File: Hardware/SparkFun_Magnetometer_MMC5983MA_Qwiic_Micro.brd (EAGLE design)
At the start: 19.1 x 8.9 mm, 35 parts, among them J1 QWIIC_RIGHT_ANGLE, U2 MMC5983MA_QFN16

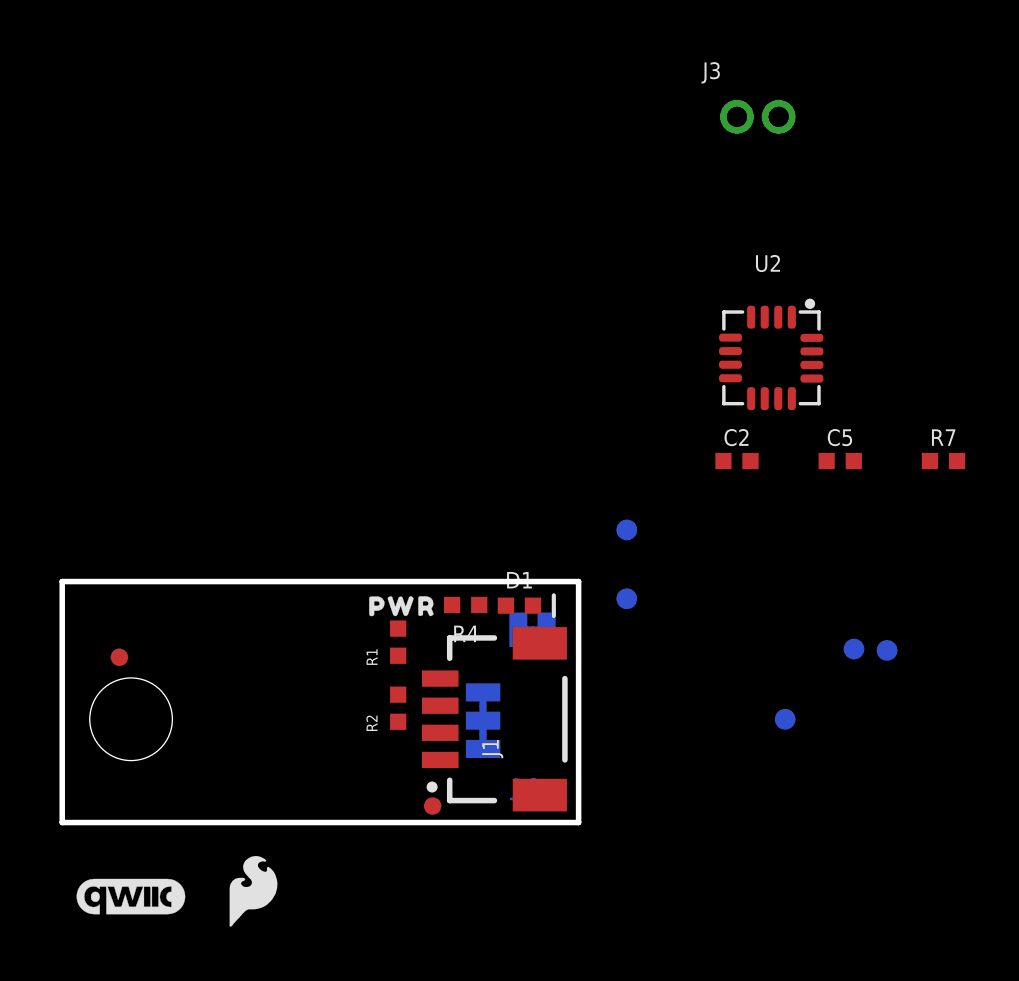
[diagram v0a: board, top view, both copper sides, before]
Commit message: Places parts, fixes some schematic alignment issues
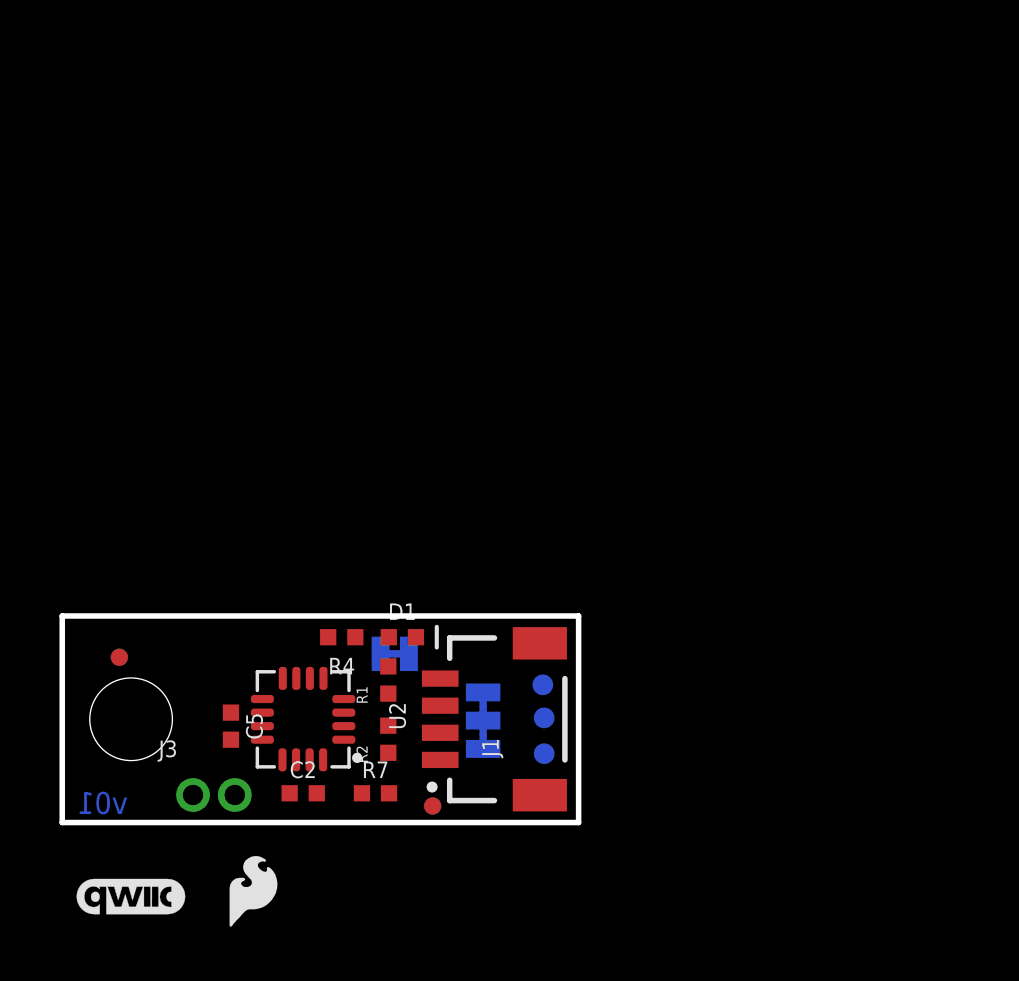
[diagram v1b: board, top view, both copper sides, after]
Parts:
- removed U$28: (no value), top:PWR8
- moved J3 32.1 mm to (4.83, 1.02)
- moved C5 24.5 mm to (6.22, 3.56), turned to 270 degrees
- moved R7 24.3 mm to (11.6, 1.08)
- moved U2 21.8 mm to (8.89, 3.81), turned to 270 degrees
- moved C2 20.2 mm to (8.89, 1.08)
- moved TP3 12.8 mm to (17.7, 5.08)
- moved TP2 11.7 mm to (17.8, 3.86)
- moved TP1 8.98 mm to (17.8, 2.54)
- moved TP5 7.85 mm to (17.8, 1.02)
- moved TP4 5.18 mm to (17.8, 6.60)
- moved LED 5.16 mm to (12.3, 6.22)
- moved R4 4.72 mm to (10.3, 6.84)
- moved D1 4.47 mm to (12.5, 6.84)
- moved R1 1.44 mm to (12.0, 5.26)
- moved R2 1.20 mm to (12.0, 3.07)
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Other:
- board size 19.1 x 8.9 mm -> 19.1 x 7.6 mm

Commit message: Adds measures
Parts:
- moved LOGO1 27.5 mm to (23.9, 14.5)
- moved U$29 27.5 mm to (28.4, 14.8)
- moved FRAME1 7.62 mm to (-18.8, -19.1)
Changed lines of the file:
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@@
 <setting verticaltext="up"/>
 </settings>
-<grid distance="0.05" unitdist="inch" unit="inch" style="dots" multiple="1" display="yes" altdistance="0.005" altunitdist="inch" altunit="inch"/>
+<grid distance="0.01" unitdist="inch" unit="inch" style="dots" multiple="1" display="yes" altdistance="0.005" altunitdist="inch" altunit="inch"/>
 <layers>
 <layer number="1" name="Top" color="4" fill="1" visible="yes" active="yes"/>
@@
 <layer number="45" name="Holes" color="7" fill="1" visible="yes" active="yes"/>
 <layer number="46" name="Milling" color="3" fill="1" visible="no" active="yes"/>
-<layer number="47" name="Measures" color="7" fill="1" visible="no" active="yes"/>
+<layer number="47" name="Measures" color="7" fill="1" visible="yes" active="yes"/>
 <layer number="48" name="Document" color="7" fill="1" visible="no" active="yes"/>
 <layer number="49" name="Reference" color="13" fill="1" visible="yes" active="yes"/>
@@
 <wire x1="19.05" y1="0" x2="19.05" y2="7.62" width="0.2032" layer="20"/>
 <text x="2.422525" y="0.314325" size="0.8128" layer="16" font="vector" ratio="22" rot="MR0">v01</text>
-<dimension x1="0" y1="8.89" x2="0" y2="0" x3="-8.636" y3="4.445" textsize="1.778" textratio="15" layer="47" unit="inch" visible="yes"/>
-<dimension x1="19.05" y1="8.89" x2="0" y2="8.89" x3="9.525" y3="22.86" textsize="1.778" textratio="15" layer="47" unit="inch" visible="yes"/>
 <rectangle x1="8.89" y1="3.4036" x2="8.9408" y2="3.7084" layer="41"/>
 <wire x1="14.2494" y1="4.752975" x2="12.3444" y2="4.752975" width="0.254" layer="22"/>
@@
 <wire x1="10.8204" y1="5.334" x2="12.0904" y2="4.064" width="0.254" layer="22"/>
 <dimension x1="13.9446" y1="3.81" x2="13.97" y2="0" x3="25.4" y3="1.905" textsize="1.778" layer="47" dtype="vertical" unit="inch"/>
-<dimension x1="2.54" y1="3.81" x2="2.54" y2="0" x3="-12.7" y3="1.905" textsize="1.778" layer="47" dtype="vertical" unit="inch"/>
-<dimension x1="6.4008" y1="7.6708" x2="0" y2="7.62" x3="3.2004" y3="11.43" textsize="1.778" layer="47" dtype="horizontal" unit="inch"/>
+<dimension x1="19.05" y1="7.62" x2="0" y2="7.62" x3="9.525" y3="16.764" textsize="1.778" layer="47" dtype="horizontal" unit="inch"/>
+<dimension x1="0" y1="7.62" x2="0" y2="0" x3="-6.096" y3="3.81" textsize="1.778" layer="47" dtype="horizontal" unit="inch"/>
+<dimension x1="8.89" y1="3.81" x2="0" y2="4.064" x3="4.445" y3="12.7" textsize="1.778" layer="47" dtype="horizontal" unit="inch"/>
+<dimension x1="2.54" y1="3.81" x2="0" y2="4.064" x3="1.27" y3="-3.302" textsize="1.778" layer="47" dtype="horizontal" unit="inch"/>
+<dimension x1="4.826" y1="1.016" x2="0" y2="1.016" x3="2.413" y3="-6.35" textsize="1.778" layer="47" dtype="horizontal" unit="inch"/>
+<dimension x1="4.826" y1="1.016" x2="4.826" y2="0" x3="-1.27" y3="0.508" textsize="1.778" layer="47" dtype="vertical" unit="inch"/>
 </plain>
 <attributes>
@@
 </autorouter>
 <elements>
-<element name="FRAME1" library="SparkFun-Aesthetics" package="CREATIVE_COMMONS" value="FRAME-LETTER" x="-19.05" y="-11.43" smashed="yes">
-<attribute name="DESIGNER" value="Elias Santistevan" x="12.7" y="-11.43" size="1.778" layer="51" font="vector"/>
-<attribute name="REV" value="" x="-19.05" y="-11.43" size="1.778" layer="27" display="off"/>
+<element name="FRAME1" library="SparkFun-Aesthetics" package="CREATIVE_COMMONS" value="FRAME-LETTER" x="-18.796" y="-19.05" smashed="yes">
+<attribute name="DESIGNER" value="Elias Santistevan" x="12.954" y="-19.05" size="1.778" layer="51" font="vector"/>
+<attribute name="REV" value="" x="-18.796" y="-19.05" size="1.778" layer="27" display="off"/>
 </element>
 <element name="LOGO2" library="SparkFun-Aesthetics" package="OSHW-LOGO-MINI" value="OSHW-LOGOMINI" x="1.4224" y="1.20015" smashed="yes" rot="MR0"/>
@@
 <element name="FD1" library="SparkFun-Aesthetics" package="FIDUCIAL-MICRO" value="FIDUCIALUFIDUCIAL" x="2.1082" y="6.096" smashed="yes" rot="MR0"/>
 <element name="FD2" library="SparkFun-Aesthetics" package="FIDUCIAL-MICRO" value="FIDUCIALUFIDUCIAL" x="13.6652" y="0.6096" smashed="yes" rot="MR0"/>
-<element name="LOGO1" library="SparkFun-Aesthetics" package="QWIIC_4MM" value="QWIIC_LOGO_4MM" x="2.54" y="-2.7432" smashed="yes"/>
+<element name="LOGO1" library="SparkFun-Aesthetics" package="QWIIC_4MM" value="QWIIC_LOGO_4MM" x="23.876" y="14.5288" smashed="yes"/>
 <element name="D1" library="ISM330DHCX" package="0402-TIGHT" value="RED" x="12.5476" y="6.838340625" smashed="yes">
 <attribute name="NAME" x="12.5476" y="7.473340625" size="0.6096" layer="25" font="vector" ratio="20" align="bottom-center"/>
@@
 <attribute name="VALUE" x="12.2682" y="7.366" size="0.6096" layer="28" font="vector" ratio="20" rot="MR180" align="top-center"/>
 </element>
-<element name="U$29" library="SparkFun-Aesthetics" package="SFE_LOGO_FLAME_.1" value="" x="7.0358" y="-2.5146" smashed="yes"/>
+<element name="U$29" library="SparkFun-Aesthetics" package="SFE_LOGO_FLAME_.1" value="" x="28.3718" y="14.7574" smashed="yes"/>
 <element name="U$8" library="ISMTopMini" package="X2114" value="" x="13.0302" y="4.0132" smashed="yes" rot="MR0"/>
 <element name="U$9" library="ISMTopMini" package="Y2115" value="" x="11.9484" y="2.9718" smashed="yes" rot="MR0"/>

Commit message: Routes the board
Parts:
- removed TP4: TEST-POINT3, SparkFun-Connectors:PAD.03X.03
- moved U$29 29.3 mm to (2.39, 1.12), turned to 90 degrees
- moved LOGO1 22.0 mm to (3.38, 6.58)
- moved FD1 1.62 mm to (0.71, 6.91)
- moved FID1 1.62 mm to (0.71, 6.91)
- moved LED 0.49 mm to (12.7, 6.50)
- moved C2 0.26 mm to (8.64, 1.03)
- moved R7 0.23 mm to (11.8, 1.03)
- moved R2 0.08 mm to (12.1, 3.15), turned to 270 degrees
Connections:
- net INT: no longer TP4.1
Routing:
- net 3.3V: track 0.00 -> 24.5 mm, vias 0 -> 4
- net SDA: track 0.00 -> 10.4 mm, vias 0 -> 1
- net SCL: track 0.00 -> 8.81 mm, vias 0 -> 1
- net !MAG_CS!: track 0.00 -> 5.37 mm, vias 0 -> 2
- net INT: track 0.00 -> 4.61 mm
- net N$5: track 0.00 -> 4.52 mm, vias 0 -> 1
- net N$6: track 0.00 -> 3.50 mm, vias 0 -> 1
- net N$3: track 0.00 -> 2.38 mm, vias 0 -> 1
- net N$2: track 0.00 -> 1.24 mm
- net GND: track 0.00 -> 0.73 mm, vias 0 -> 6
- added copper zone on layer 1, net 3.3V
- added copper zone on layer 1, net CAP

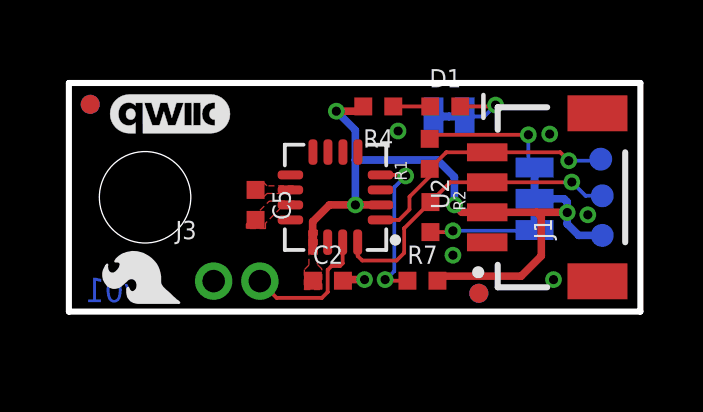
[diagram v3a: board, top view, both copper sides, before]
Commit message: Adds Silk, moves testpoints to grid, updates two pin connector
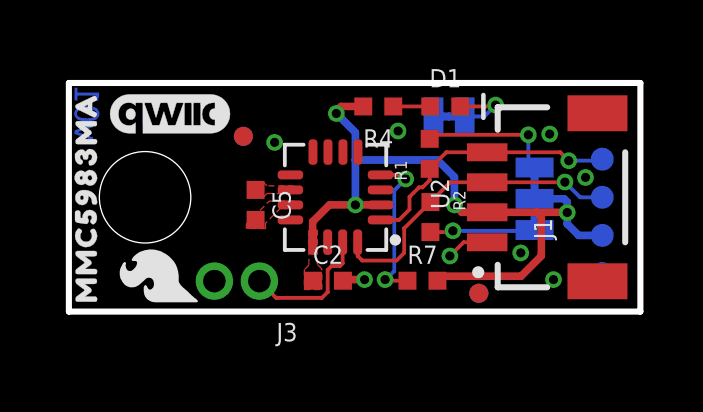
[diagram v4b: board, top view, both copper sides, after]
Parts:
- removed LOGO3: SFE_LOGO_NAMEBLANK, SparkFun-Aesthetics:BLANK
- added U$1, U$2: (no value), topMini:MMC5983MA331
- moved FD1 5.22 mm to (5.82, 5.84)
- moved FID1 5.22 mm to (5.82, 5.84)
- moved U$5 5.09 mm to (4.88, 2.91), turned to 90 degrees
- moved U$6 3.90 mm to (6.30, 2.71), turned to 90 degrees
- moved U$8 3.70 mm to (9.45, 4.95), turned to 270 degrees
- moved U$9 3.21 mm to (8.74, 2.81), turned to 90 degrees
- moved U$3 3.03 mm to (14.1, 3.84)
- moved U$10 2.45 mm to (11.6, 3.61), turned to 90 degrees
- moved J3 1.52 mm to (6.35, 1.02), turned to 180 degrees
- moved U$4 0.71 mm to (15.3, 6.60), turned to 180 degrees
- moved U$29 0.59 mm to (2.97, 1.17)
- moved TP5 0.25 mm to (17.8, 1.27)
- moved TP3 0.05 mm to (17.8, 5.08)
- moved TP2 0.05 mm to (17.8, 3.81)
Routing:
- net GND: track 0.73 -> 2.17 mm, vias 6 -> 8

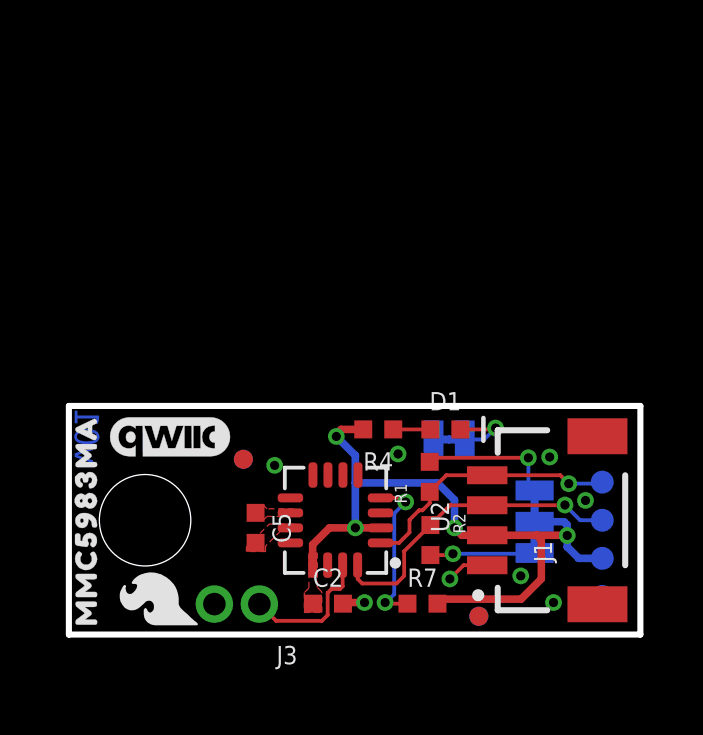
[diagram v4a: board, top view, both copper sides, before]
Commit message: Moves interrupt and ground pins, fixes silk, moves testpoints to 0.0375" grid
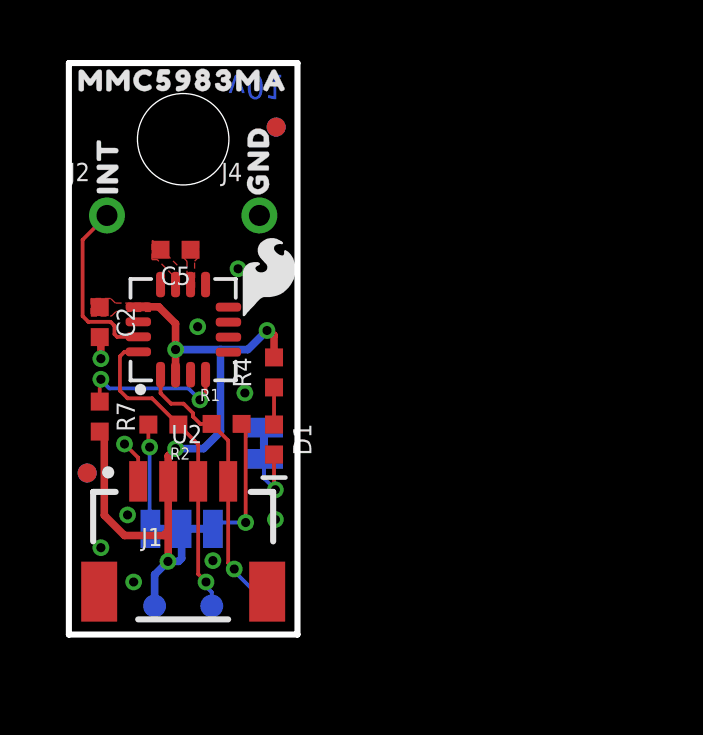
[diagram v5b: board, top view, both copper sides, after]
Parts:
- removed J3: (no value), SparkFun-Connectors:1X02_1.5MM_NO_SILK
- added J2, J4: (no value), SparkFun-Connectors:1X01_1MM_NO_SILK
- U$4: device LISMini:#LED#7 -> topMini:#LED#15
- moved TP5 16.8 mm to (0.95, 0.95), turned to 90 degrees
- moved LOGO2 16.4 mm to (1.20, 17.6), turned to 90 degrees
- moved TP1 15.0 mm to (2.86, 0.95), turned to 90 degrees
- moved U$1 15.0 mm to (3.81, 18.5), turned to 0 degrees
- moved FD2 13.9 mm to (0.61, 5.38), turned to 90 degrees
- moved FID2 13.9 mm to (0.61, 5.38), turned to 270 degrees
- moved U$6 13.9 mm to (1.29, 15.6), flipped to the top
- moved TP2 13.3 mm to (4.76, 0.95), turned to 90 degrees
- moved U$5 13.0 mm to (6.32, 15.8), flipped to the top
- moved STANDOFF3 12.8 mm to (3.81, 16.5), turned to 270 degrees
- moved R7 12.4 mm to (1.03, 7.26), turned to 270 degrees
- moved C2 12.1 mm to (1.03, 10.4), turned to 270 degrees
- moved TP3 11.9 mm to (6.67, 0.95), turned to 90 degrees
- moved I2C_PU 11.8 mm to (3.76, 3.52), turned to 0 degrees
- moved U$29 11.4 mm to (6.65, 11.9), turned to 0 degrees
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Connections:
- net GND: now also J4.1; no longer J3.1
- net INT: now also J2.1; no longer J3.2
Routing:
- net INT: track 4.62 -> 6.00 mm
- net SCL: track 8.93 -> 9.67 mm
- net GND: vias 8 -> 10
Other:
- board size 19.1 x 7.6 mm -> 7.6 x 19.1 mm
